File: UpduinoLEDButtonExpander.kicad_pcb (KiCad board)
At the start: 2 copper layers, 50 x 50 mm, 23 parts, among them J1 Upduino2, J2 Upduino2, J3 Upduino2, SW1 BTN, SW2 BTN, SW3 BTN, SW4 BTN

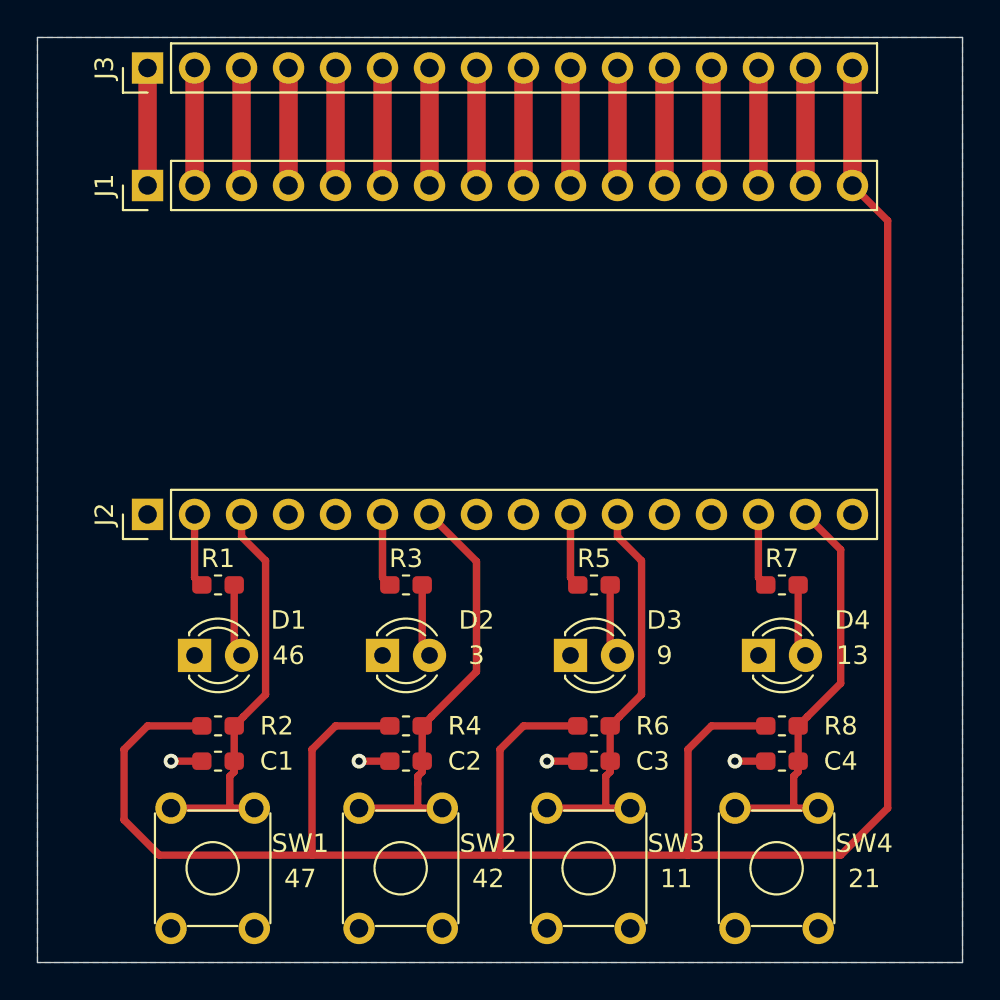
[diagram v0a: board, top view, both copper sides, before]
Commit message: Added additional protection resistor for the buttons
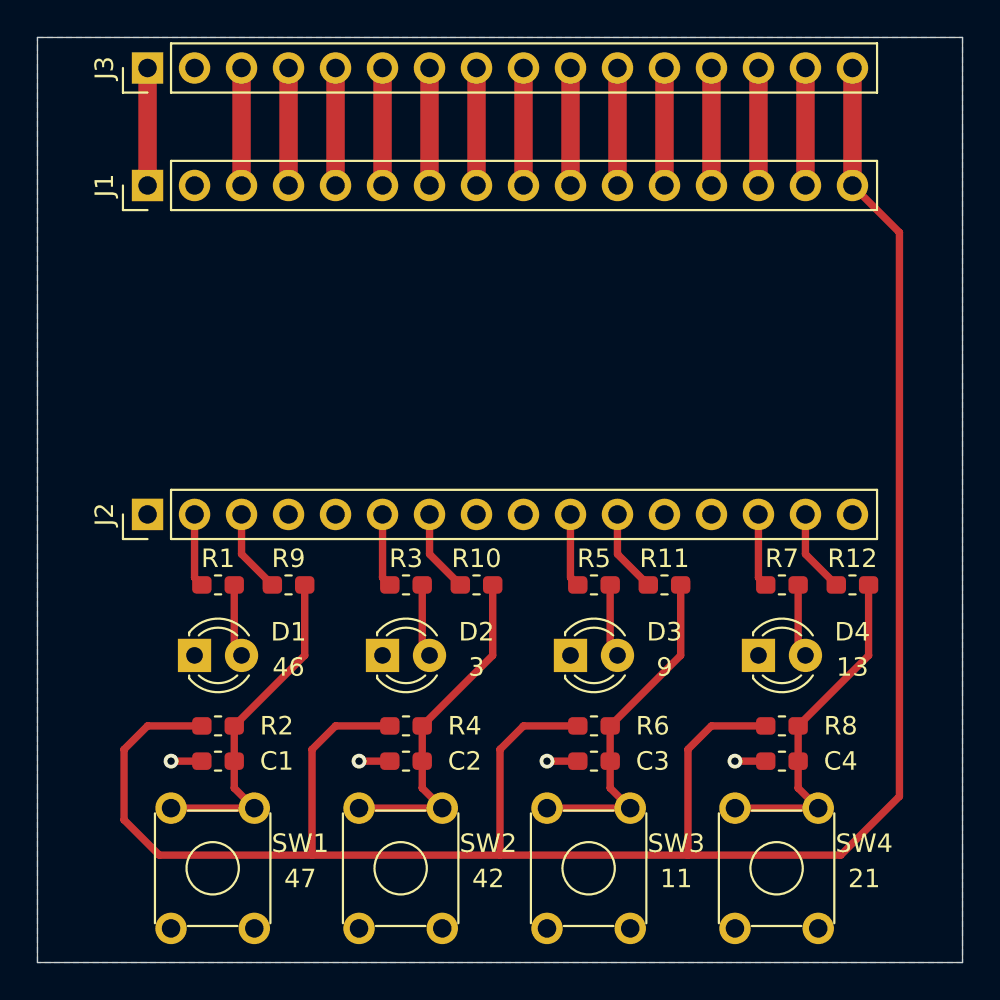
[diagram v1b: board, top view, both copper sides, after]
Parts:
- added R10: 220, Resistor_SMD:R_0603_1608Metric_Pad1.05x0.95mm_HandSolder, F.Cu at (142.2, 92.7)
- added R11: 220, Resistor_SMD:R_0603_1608Metric_Pad1.05x0.95mm_HandSolder, F.Cu at (152.4, 92.7)
- added R12: 220, Resistor_SMD:R_0603_1608Metric_Pad1.05x0.95mm_HandSolder, F.Cu at (162.6, 92.7)
- added R9: 220, Resistor_SMD:R_0603_1608Metric_Pad1.05x0.95mm_HandSolder, F.Cu at (132.1, 92.7)
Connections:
- C1 pad 1: /47 -> Net-(C1-Pad1)
- C2 pad 1: /4 -> Net-(C2-Pad1)
- C3 pad 1: /11 -> Net-(C3-Pad1)
- C4 pad 1: /21 -> Net-(C4-Pad1)
- R2 pad 1: /47 -> Net-(C1-Pad1)
- R4 pad 1: /4 -> Net-(C2-Pad1)
- R6 pad 1: /11 -> Net-(C3-Pad1)
- R8 pad 1: /21 -> Net-(C4-Pad1)
- SW1 pad 2: /47 -> Net-(C1-Pad1)
- SW1 pad 4: /47 -> Net-(C1-Pad1)
- SW2 pad 2: /4 -> Net-(C2-Pad1)
- SW2 pad 4: /4 -> Net-(C2-Pad1)
- SW3 pad 2: /11 -> Net-(C3-Pad1)
- SW3 pad 4: /11 -> Net-(C3-Pad1)
- SW4 pad 2: /21 -> Net-(C4-Pad1)
- SW4 pad 4: /21 -> Net-(C4-Pad1)
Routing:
- net Net-(C4-Pad1): track 0.00 -> 18.6 mm
- net Net-(C3-Pad1): track 0.00 -> 18.6 mm
- net Net-(C2-Pad1): track 0.00 -> 18.6 mm
- net Net-(C1-Pad1): track 0.00 -> 18.6 mm
- net /4: track 22.7 -> 4.50 mm
- net /21: track 22.2 -> 4.50 mm
- net /11: track 21.7 -> 4.50 mm
- net /47: track 21.7 -> 4.50 mm
- net /38: track 6.35 -> 0.00 mm
- net +3V3: track 123.8 -> 124.3 mm

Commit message: Updated pdf files
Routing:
- net /38: track 0.00 -> 6.35 mm
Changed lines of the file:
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@@
     (thickness 1.6)
     (drawings 12)
-    (tracks 91)
+    (tracks 92)
     (zones 0)
     (modules 27)
@@
   )
   (setup
-    (last_trace_width 0.4)
+    (last_trace_width 1)
     (user_trace_width 0.4)
     (user_trace_width 1)
@@
   (segment (start 159.625 92.71) (end 159.625 96.125) (width 0.4) (layer F.Cu) (net 7) (status 30))
   (segment (start 124.46 71.12) (end 124.46 64.77) (width 1) (layer F.Cu) (net 8) (status 30))
+  (segment (start 127 64.77) (end 127 71.12) (width 1) (layer F.Cu) (net 9))
   (segment (start 129.54 71.12) (end 129.54 64.77) (width 1) (layer F.Cu) (net 10) (status 30))
   (segment (start 132.08 64.77) (end 132.08 71.12) (width 1) (layer F.Cu) (net 11) (status 30))

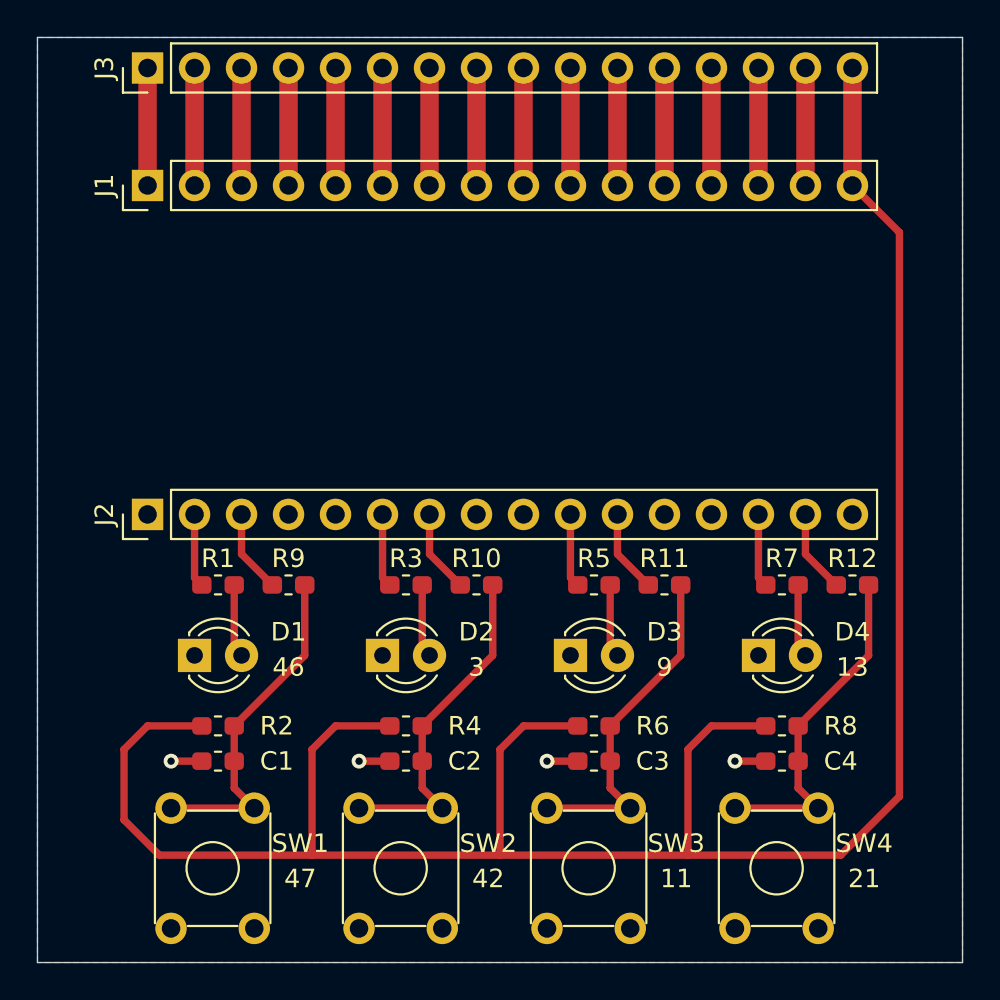
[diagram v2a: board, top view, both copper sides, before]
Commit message: Corrected button symbol, added more labels
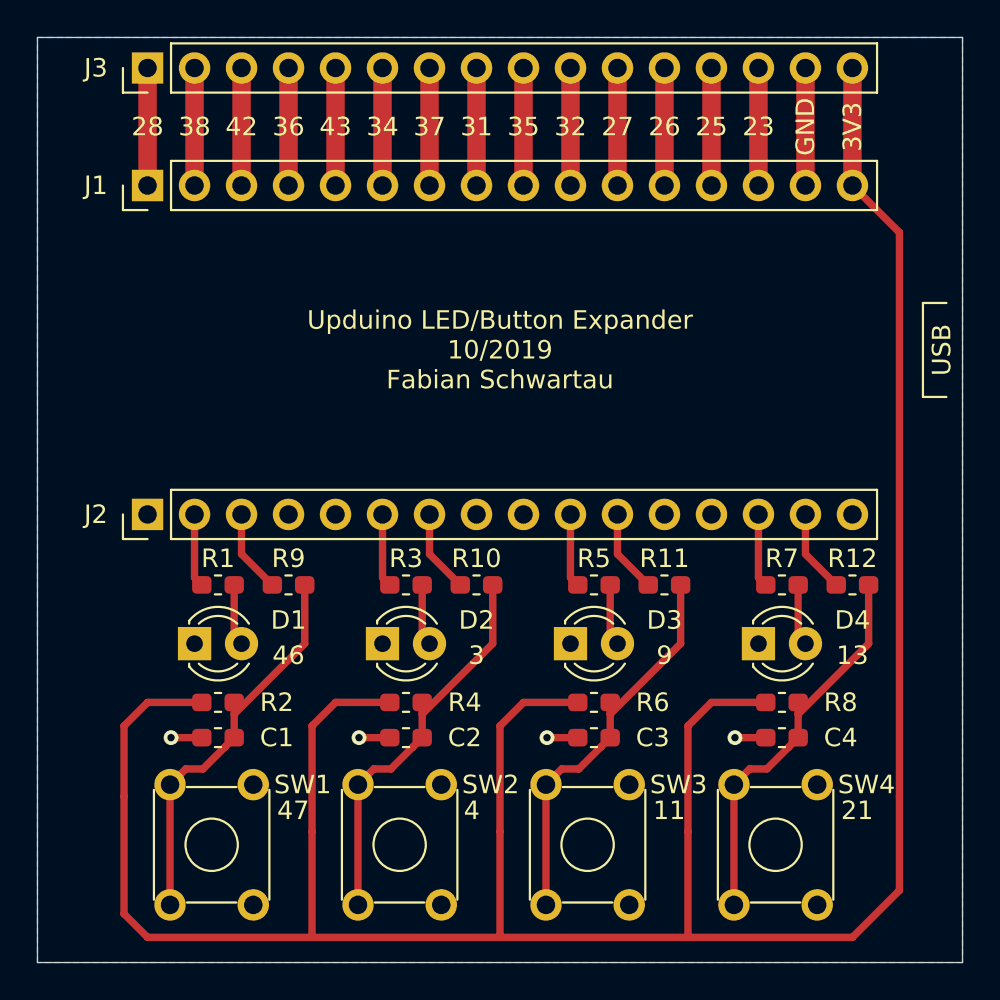
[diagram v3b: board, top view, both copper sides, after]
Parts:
- SW1, SW2, SW3, SW4: value BTN -> SW_Push_Dual
- moved SW2 8.95 mm to (140.3, 103.5), turned to 270 degrees
- moved SW1 8.95 mm to (130.2, 103.5), turned to 270 degrees
- moved SW3 8.95 mm to (150.5, 103.5), turned to 270 degrees
- moved SW4 8.95 mm to (160.7, 103.5), turned to 270 degrees
- moved C1 1.27 mm to (128.3, 101.0)
- moved C2 1.27 mm to (138.4, 101.0)
- moved C3 1.27 mm to (148.6, 101.0)
- moved C4 1.27 mm to (158.8, 101.0)
- moved R2 1.27 mm to (128.3, 99.1)
- moved R4 1.27 mm to (138.4, 99.1)
- moved R6 1.27 mm to (148.6, 99.1)
- moved R8 1.27 mm to (158.8, 99.1)
- moved D1 0.63 mm to (127.0, 95.9)
- moved D2 0.63 mm to (137.2, 95.9)
- moved D3 0.63 mm to (147.3, 95.9)
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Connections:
- SW1 pad 2: Net-(C1-Pad1) -> GND
- SW1 pad 3: GND -> Net-(C1-Pad1)
- SW2 pad 2: Net-(C2-Pad1) -> GND
- SW2 pad 3: GND -> Net-(C2-Pad1)
- SW3 pad 2: Net-(C3-Pad1) -> GND
- SW3 pad 3: GND -> Net-(C3-Pad1)
- SW4 pad 2: Net-(C4-Pad1) -> GND
- SW4 pad 3: GND -> Net-(C4-Pad1)
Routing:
- net +3V3: track 124.3 -> 152.4 mm
- net Net-(C1-Pad1): track 18.6 -> 21.5 mm
- net Net-(C2-Pad1): track 18.6 -> 21.5 mm
- net Net-(C4-Pad1): track 18.6 -> 21.5 mm
- net Net-(C3-Pad1): track 18.6 -> 21.5 mm
- net Net-(D2-Pad2): track 3.97 -> 3.34 mm
- net Net-(D1-Pad2): track 3.97 -> 3.34 mm
- net Net-(D4-Pad2): track 3.97 -> 3.34 mm
- net Net-(D3-Pad2): track 3.97 -> 3.34 mm
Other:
- board text added: "23"
- board text added: "25"
- board text added: "26"
- board text added: "27"
- board text added: "28"
- board text added: "31"
- board text added: "32"
- board text added: "34"
- board text added: "35"
- board text added: "36"
- board text added: "37"
- board text added: "38"
- board text added: "3V3"
- board text added: "4"
- board text added: "43"
- board text added: "GND"
- board text added: "USB"
- board text added: "Upduino LED/Button Expander 10/2019 Fabian Schwartau"
